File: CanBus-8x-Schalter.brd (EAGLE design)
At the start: 80 x 80 mm, 68 parts, among them IC1 LM2937IMP-5.0, IC2 ATMEGA1284P, IC3 MCP2515T-I/SO, IC4 MCP2562-E/SN, K1 36.11, K2 36.11, K3 36.11, K4 36.11, K5 36.11, K6 36.11, K7 36.11, K8 36.11, Q1 EUROQUARTZ-MMJ, Q2 EUROQUARTZ-MMJ, X1 MKDSN1,5/3-5,08, X2 MKDSN1,5/3-5,08, X3 MKDSN1,5/3-5,08, X4 MKDSN1,5/3-5,08, X5 MKDSN1,5/3-5,08, X6 MKDSN1,5/3-5,08, X7 MKDSN1,5/3-5,08, X8 MKDSN1,5/3-5,08

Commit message: Werte von Bauteilen angepasst
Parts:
- C1: value (none) -> 100nF
- C10, C11, C12, C13, C14, C15, C16, C17: value 100n -> 100nF
- C2: value (none) -> 10µF Low ESR
- Q1, Q2: value EUROQUARTZ-MMJ -> 16MHz
- RN1, RN2, RN3, RN4: value (none) -> 10k
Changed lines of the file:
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@@
 </autorouter>
 <elements>
-<element name="C1" library="rcl" package="C0805" value="" x="59.69" y="39.6875" smashed="yes" rot="R180">
+<element name="C1" library="rcl" package="C0805" value="100nF" x="59.69" y="39.6875" smashed="yes" rot="R180">
 <attribute name="NAME" x="61.2775" y="38.735" size="0.8128" layer="25" font="vector" align="top-right"/>
 <attribute name="VALUE" x="60.96" y="42.2275" size="1.27" layer="27" rot="R180"/>
 </element>
-<element name="C2" library="rcl" package="C0805" value="" x="59.69" y="48.5775" smashed="yes" rot="R180">
+<element name="C2" library="rcl" package="C0805" value="10µF Low ESR" x="59.69" y="48.5775" smashed="yes" rot="R180">
 <attribute name="NAME" x="61.595" y="48.5775" size="0.8128" layer="25" font="vector" align="center-left"/>
 <attribute name="VALUE" x="60.96" y="51.1175" size="1.27" layer="27" rot="R180"/>
@@
 <attribute name="NAME" x="58.674" y="36.195" size="0.8128" layer="25" font="vector" rot="R90"/>
 </element>
-<element name="Q1" library="crystal-smd" package="MJ-5X3.2" value="EUROQUARTZ-MMJ" x="25.273" y="32.4485" smashed="yes">
+<element name="Q1" library="crystal-smd" package="MJ-5X3.2" value="16MHz" x="25.273" y="32.4485" smashed="yes">
 <attribute name="REICHELT" value="16,000000-MJ" x="25.273" y="32.4485" size="1.778" layer="27" display="off"/>
 <attribute name="NAME" x="25.2355" y="30.456" size="0.8128" layer="25" font="vector" align="top-center"/>
@@
 <attribute name="VALUE" x="26.67" y="33.7185" size="1.27" layer="27" rot="R270"/>
 </element>
-<element name="Q2" library="crystal-smd" package="MJ-5X3.2" value="EUROQUARTZ-MMJ" x="47.625" y="47.117" smashed="yes">
+<element name="Q2" library="crystal-smd" package="MJ-5X3.2" value="16MHz" x="47.625" y="47.117" smashed="yes">
 <attribute name="REICHELT" value="16,000000-MJ" x="38.735" y="56.007" size="1.778" layer="27" display="off"/>
 <attribute name="NAME" x="47.5875" y="48.9345" size="0.8128" layer="25" font="vector" align="bottom-center"/>
@@
 <attribute name="VALUE" x="40.9575" y="29.21" size="1.27" layer="27"/>
 </element>
-<element name="RN1" library="resistor-dil" package="0603-ARC" value="" x="8.89" y="32.0675" smashed="yes" rot="R270">
+<element name="RN1" library="resistor-dil" package="0603-ARC" value="10k" x="8.89" y="32.0675" smashed="yes" rot="R270">
 <attribute name="OC_NEWARK" value="unknown" x="8.89" y="32.0675" size="1.778" layer="27" rot="R270" display="off"/>
 <attribute name="OC_FARNELL" value="unknown" x="8.89" y="32.0675" size="1.778" layer="27" rot="R270" display="off"/>
@@
 <attribute name="VALUE" x="10.16" y="33.9725" size="1.27" layer="27" ratio="10" rot="R270"/>
 </element>
-<element name="C10" library="rcl" package="C0805" value="100n" x="8.255" y="33.02" smashed="yes" rot="MR0">
+<element name="C10" library="rcl" package="C0805" value="100nF" x="8.255" y="33.02" smashed="yes" rot="MR0">
 <attribute name="NAME" x="10.795" y="33.02" size="0.8128" layer="26" font="vector" rot="MR0" align="center-right"/>
 <attribute name="VALUE" x="9.525" y="30.48" size="1.27" layer="28" rot="MR0"/>
 </element>
-<element name="C11" library="rcl" package="C0805" value="100n" x="8.255" y="31.115" smashed="yes" rot="MR0">
+<element name="C11" library="rcl" package="C0805" value="100nF" x="8.255" y="31.115" smashed="yes" rot="MR0">
 <attribute name="NAME" x="10.795" y="31.115" size="0.8128" layer="26" font="vector" rot="MR0" align="center-right"/>
 <attribute name="VALUE" x="9.525" y="28.575" size="1.27" layer="28" rot="MR0"/>
@@
 <attribute name="VALUE" x="64.4525" y="8.255" size="1.27" layer="27"/>
 </element>
-<element name="RN2" library="resistor-dil" package="0603-ARC" value="" x="8.89" y="37.1475" smashed="yes" rot="R270">
+<element name="RN2" library="resistor-dil" package="0603-ARC" value="10k" x="8.89" y="37.1475" smashed="yes" rot="R270">
 <attribute name="MF" value="" x="11.43" y="37.1475" size="1.27" layer="27" ratio="15" rot="R270" display="off"/>
 <attribute name="MPN" value="" x="11.43" y="37.1475" size="1.27" layer="27" ratio="15" rot="R270" display="off"/>
@@
 <attribute name="VALUE" x="10.16" y="39.0525" size="1.27" layer="27" ratio="10" rot="R270"/>
 </element>
-<element name="C12" library="rcl" package="C0805" value="100n" x="8.255" y="38.1" smashed="yes" rot="MR0">
+<element name="C12" library="rcl" package="C0805" value="100nF" x="8.255" y="38.1" smashed="yes" rot="MR0">
 <attribute name="NAME" x="10.795" y="38.1" size="0.8128" layer="26" font="vector" rot="MR0" align="center-right"/>
 <attribute name="VALUE" x="9.525" y="35.56" size="1.27" layer="28" rot="MR0"/>
 </element>
-<element name="C13" library="rcl" package="C0805" value="100n" x="8.255" y="36.195" smashed="yes" rot="MR0">
+<element name="C13" library="rcl" package="C0805" value="100nF" x="8.255" y="36.195" smashed="yes" rot="MR0">
 <attribute name="NAME" x="10.795" y="36.195" size="0.8128" layer="26" font="vector" rot="MR0" align="center-right"/>
 <attribute name="VALUE" x="9.525" y="33.655" size="1.27" layer="28" rot="MR0"/>
@@
 <attribute name="NAME" x="42.799" y="40.767" size="0.8128" layer="26" font="vector" rot="MR180"/>
 </element>
-<element name="RN3" library="resistor-dil" package="0603-ARC" value="" x="8.89" y="42.8625" smashed="yes" rot="R270">
+<element name="RN3" library="resistor-dil" package="0603-ARC" value="10k" x="8.89" y="42.8625" smashed="yes" rot="R270">
 <attribute name="OC_FARNELL" value="unknown" x="24.13" y="49.2125" size="1.778" layer="27" rot="R270" display="off"/>
 <attribute name="OC_NEWARK" value="unknown" x="24.13" y="49.2125" size="1.778" layer="27" rot="R270" display="off"/>
@@
 <attribute name="VALUE" x="10.16" y="44.7675" size="1.27" layer="27" ratio="10" rot="R270"/>
 </element>
-<element name="C14" library="rcl" package="C0805" value="100n" x="8.255" y="43.815" smashed="yes" rot="MR0">
+<element name="C14" library="rcl" package="C0805" value="100nF" x="8.255" y="43.815" smashed="yes" rot="MR0">
 <attribute name="NAME" x="10.795" y="43.815" size="0.8128" layer="26" font="vector" rot="MR0" align="center-right"/>
 <attribute name="VALUE" x="9.525" y="41.275" size="1.27" layer="28" rot="MR0"/>
 </element>
-<element name="C15" library="rcl" package="C0805" value="100n" x="8.255" y="41.91" smashed="yes" rot="MR0">
+<element name="C15" library="rcl" package="C0805" value="100nF" x="8.255" y="41.91" smashed="yes" rot="MR0">
 <attribute name="NAME" x="10.795" y="41.91" size="0.8128" layer="26" font="vector" rot="MR0" align="center-right"/>
 <attribute name="VALUE" x="9.525" y="39.37" size="1.27" layer="28" rot="MR0"/>
 </element>
-<element name="RN4" library="resistor-dil" package="0603-ARC" value="" x="8.89" y="47.9425" smashed="yes" rot="R270">
+<element name="RN4" library="resistor-dil" package="0603-ARC" value="10k" x="8.89" y="47.9425" smashed="yes" rot="R270">
 <attribute name="OC_FARNELL" value="unknown" x="-5.08" y="59.3725" size="1.778" layer="27" rot="R270" display="off"/>
 <attribute name="OC_NEWARK" value="unknown" x="-5.08" y="59.3725" size="1.778" layer="27" rot="R270" display="off"/>
@@
 <attribute name="VALUE" x="10.16" y="49.8475" size="1.27" layer="27" ratio="10" rot="R270"/>
 </element>
-<element name="C16" library="rcl" package="C0805" value="100n" x="8.255" y="48.895" smashed="yes" rot="MR0">
+<element name="C16" library="rcl" package="C0805" value="100nF" x="8.255" y="48.895" smashed="yes" rot="MR0">
 <attribute name="NAME" x="10.795" y="48.895" size="0.8128" layer="26" font="vector" rot="MR0" align="center-right"/>
 <attribute name="VALUE" x="9.525" y="46.355" size="1.27" layer="28" rot="MR0"/>
 </element>
-<element name="C17" library="rcl" package="C0805" value="100n" x="8.255" y="46.99" smashed="yes" rot="MR0">
+<element name="C17" library="rcl" package="C0805" value="100nF" x="8.255" y="46.99" smashed="yes" rot="MR0">
 <attribute name="NAME" x="10.795" y="46.99" size="0.8128" layer="26" font="vector" rot="MR0" align="center-right"/>
 <attribute name="VALUE" x="9.525" y="44.45" size="1.27" layer="28" rot="MR0"/>

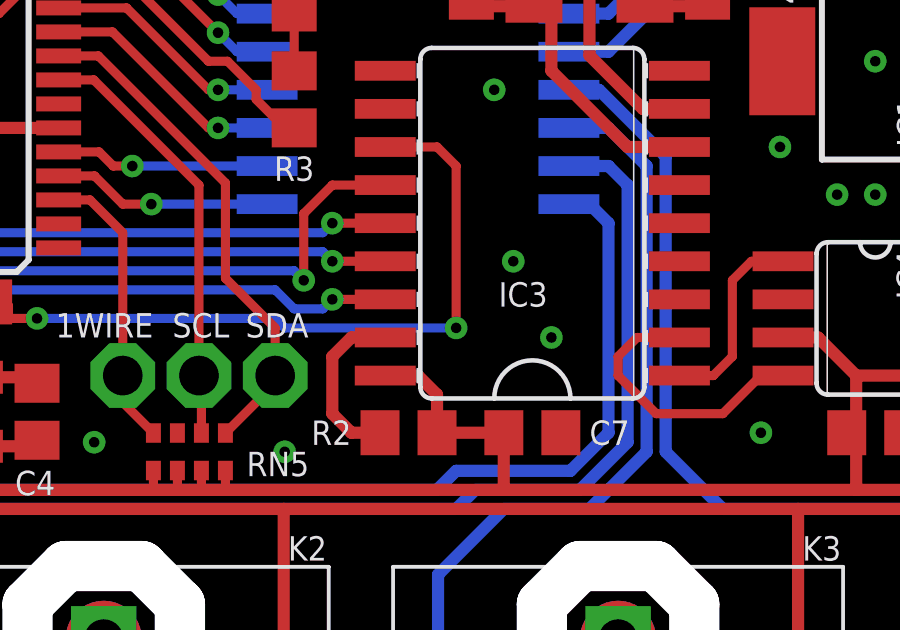
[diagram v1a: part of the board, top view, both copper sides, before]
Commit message: CAN-Bus 8x-Schalter CS PullUp hinzugefügt
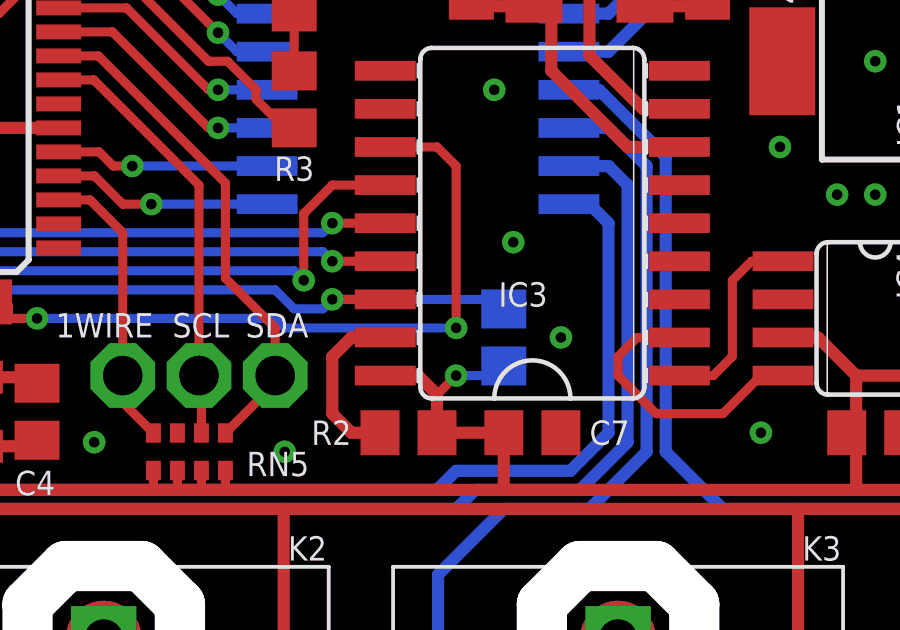
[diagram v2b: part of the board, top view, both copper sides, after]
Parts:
- added R4: 4,7k, rcl:R0805
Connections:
- net +5V: now also R4.2
- net CS: now also R4.1
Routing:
- net CS: track 24.0 -> 29.9 mm
- net +5V: track 198.3 -> 200.9 mm, vias 5 -> 6
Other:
- board text added: "CAN-Bus 8x-Schalter Rev 2024/06 (c) Peter Müller cryCode.de"
- board text removed: "CAN-Bus 8x-Schalter Rev 2020/04 (c) Peter Müller cryCode.de"
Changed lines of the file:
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@@
 <?xml version="1.0" encoding="utf-8"?>
 <!DOCTYPE eagle SYSTEM "eagle.dtd">
-<eagle version="7.4.0">
+<eagle version="7.7.0">
 <drawing>
 <settings>
@@
 <text x="22.86" y="46.99" size="1.016" layer="22" font="vector" ratio="10" rot="MR0" align="center">CAN-Bus
 8x-Schalter
-Rev 2020/04
+Rev 2024/06
 (c) Peter Müller
 cryCode.de</text>
@@
 <attribute name="VALUE" x="40.3225" y="46.355" size="1.27" layer="27" rot="R90"/>
 </element>
+<element name="R4" library="rcl" package="R0805" value="4,7k" x="44.7675" y="34.925" smashed="yes" rot="MR270">
+<attribute name="NAME" x="43.4975" y="36.83" size="0.8128" layer="26" font="vector" rot="MR0" align="top-left"/>
+<attribute name="VALUE" x="47.3075" y="35.56" size="1.27" layer="28" rot="MR270"/>
+</element>
 </elements>
 <signals>
@@
 <via x="53.975" y="41.275" extent="1-16" drill="0.35" diameter="0.7"/>
 <via x="41.275" y="46.6725" extent="1-16" drill="0.35" diameter="0.7"/>
-<via x="46.355" y="34.925" extent="1-16" drill="0.35" diameter="0.7"/>
+<via x="46.6725" y="34.925" extent="1-16" drill="0.35" diameter="0.7"/>
 <via x="37.465" y="31.115" extent="1-16" drill="0.35" diameter="0.7"/>
 <via x="60.96" y="31.75" extent="1-16" drill="0.35" diameter="0.7"/>
@@
 <via x="55.88" y="48.5775" extent="1-16" drill="0.35" diameter="0.7"/>
 <via x="55.88" y="39.6875" extent="1-16" drill="0.35" diameter="0.7"/>
-<via x="45.085" y="37.465" extent="1-16" drill="0.35" diameter="0.7"/>
+<via x="45.085" y="38.1" extent="1-16" drill="0.35" diameter="0.7"/>
 <via x="16.8275" y="41.5925" extent="1-16" drill="0.35" diameter="0.7"/>
 <via x="14.605" y="36.5125" extent="1-16" drill="0.35" diameter="0.7"/>
@@
 <wire x1="14.2875" y1="29.845" x2="13.6525" y2="30.48" width="0.4064" layer="1"/>
 <wire x1="15.875" y1="34.29" x2="13.6525" y2="34.29" width="0.4064" layer="1"/>
+<contactref element="R4" pad="2"/>
+<wire x1="44.7675" y1="33.975" x2="44.4475" y2="33.655" width="0.3048" layer="16"/>
+<wire x1="44.4475" y1="33.655" x2="43.18" y2="33.655" width="0.3048" layer="16"/>
+<via x="43.18" y="33.655" extent="1-16" drill="0.35" diameter="0.7"/>
+<wire x1="43.18" y1="33.655" x2="42.5475" y2="33.0225" width="0.3048" layer="1"/>
+<wire x1="42.5475" y1="33.0225" x2="42.5425" y2="33.0225" width="0.3048" layer="1"/>
 </signal>
 <signal name="CANL">
@@
 <wire x1="37.7825" y1="35.8775" x2="37.1475" y2="36.5125" width="0.3048" layer="16"/>
 <wire x1="37.1475" y1="36.5125" x2="23.8125" y2="36.5125" width="0.3048" layer="16"/>
+<contactref element="R4" pad="1"/>
+<wire x1="44.7675" y1="35.875" x2="44.4475" y2="36.195" width="0.3048" layer="16"/>
+<wire x1="44.4475" y1="36.195" x2="39.0525" y2="36.195" width="0.3048" layer="16"/>
 </signal>
 <signal name="INT">
